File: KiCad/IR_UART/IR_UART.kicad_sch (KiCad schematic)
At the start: 23 parts, among them J1 Conn_01x04, J2 Mounting PTH, J3 Mounting PTH, J4 Mounting PTH, J5 Mounting PTH, Q1 BC817, U1 TSDP34156, U2 74HC132

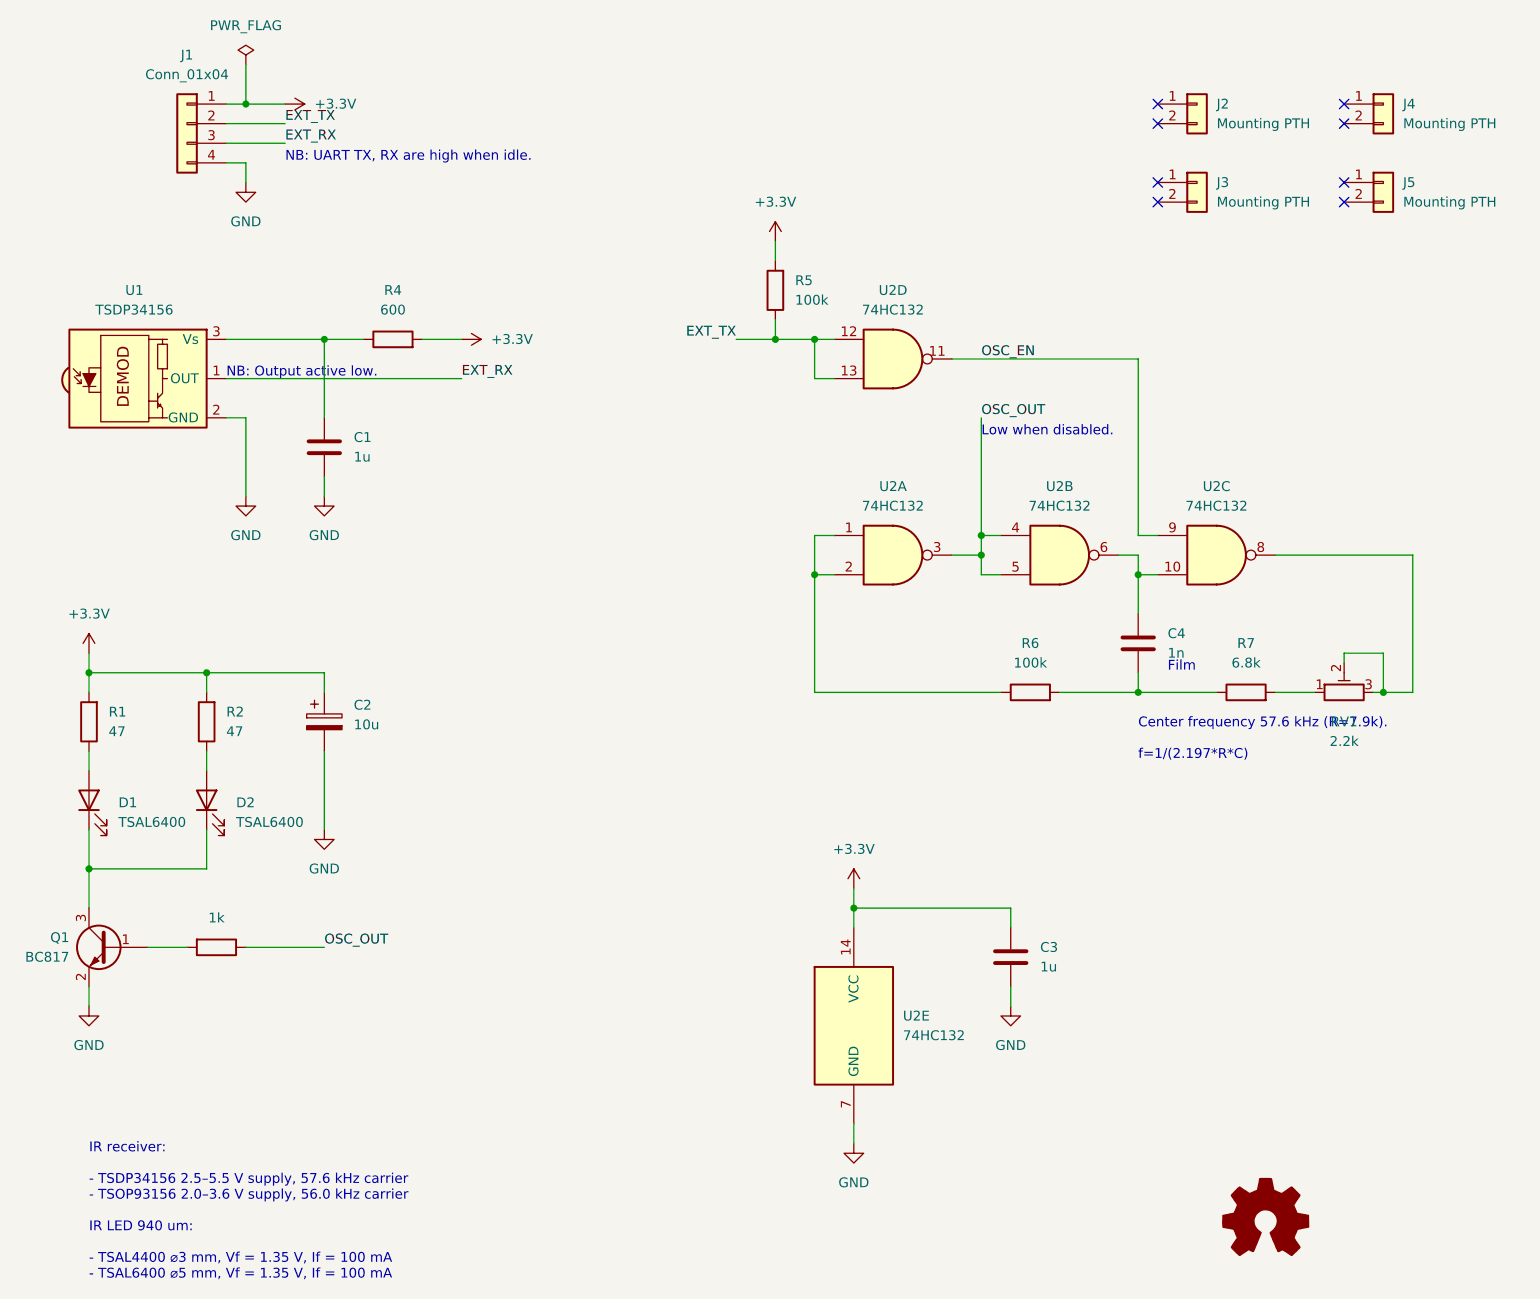
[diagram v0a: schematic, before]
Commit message: Update the schematic and the PCB
- Use 4.7k resistor instead of 6.8k in the timing circuit
- Minor changes to the board, mainly aroung the 4-pin connector
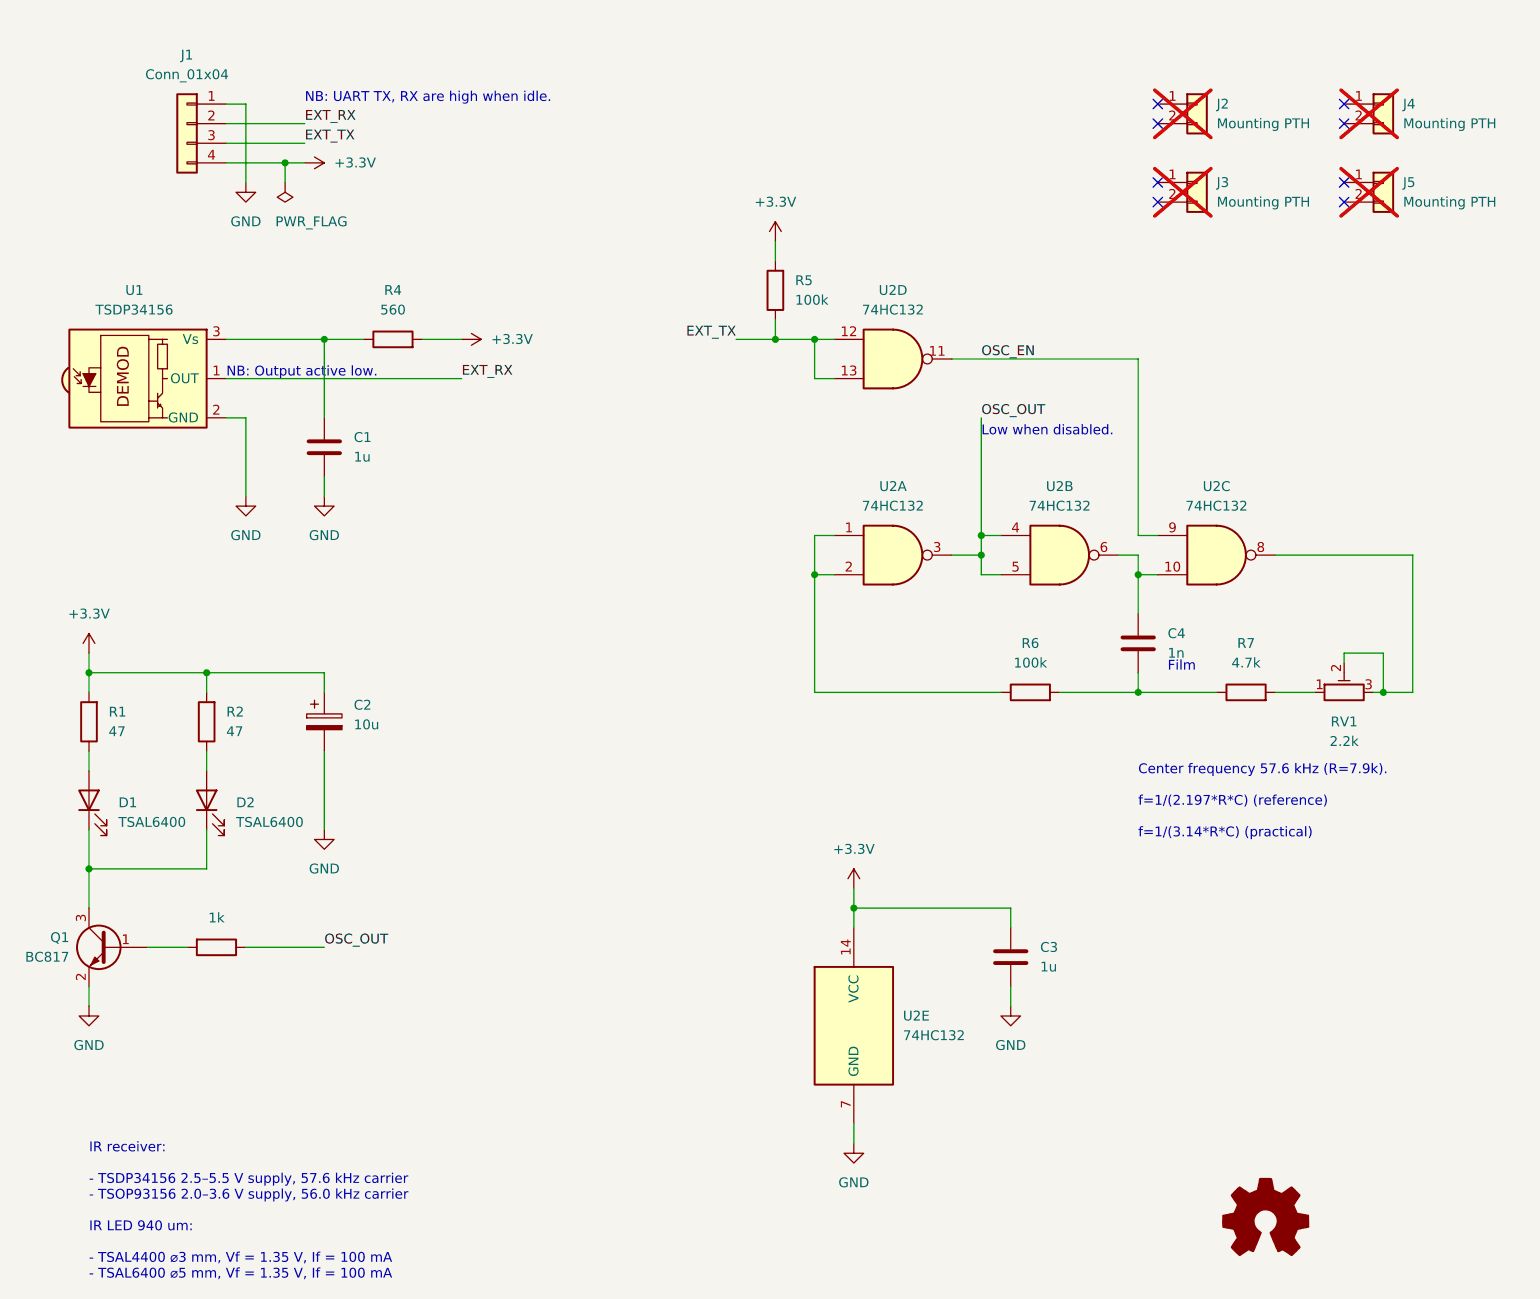
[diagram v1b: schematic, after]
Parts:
- J2, J3, J4, J5: now not fitted; now left out of the parts list
- R4: value 600 -> 560
- R7: value 6.8k -> 4.7k
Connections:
- net +3.3V: now also J1.4 (Pin_4); no longer J1.1 (Pin_1)
- net EXT_RX: now also J1.2 (Pin_2); no longer J1.3 (Pin_3)
- net EXT_TX: now also J1.3 (Pin_3); no longer J1.2 (Pin_2)
- net GND: now also J1.1 (Pin_1); no longer J1.4 (Pin_4)
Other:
- note added: "Center frequency 57.6 kHz (R=7.9k). f=1/(2.197*R*C) (reference) f=1/(3.14*R*C) (practical)"
- note removed: "Center frequency 57.6 kHz (R=7.9k). f=1/(2.197*R*C)"
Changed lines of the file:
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@@
   (title_block
     (title "IR UART 9600 baud")
-    (rev "1")
+    (rev "1.1")
   )
   (junction (at 46.99 102.87) (diameter 0) (color 0 0 0 0)
   )
-  (junction (at 52.07 29.21) (diameter 0) (color 0 0 0 0)
-  )
   (junction (at 62.23 59.69) (diameter 0) (color 0 0 0 0)
   )
@@
   )
   (junction (at 147.32 85.09) (diameter 0) (color 0 0 0 0)
+  )
+  (junction (at 57.15 36.83) (diameter 0) (color 0 0 0 0)
   )
   (junction (at 31.75 102.87) (diameter 0) (color 0 0 0 0)
@@
     (stroke (width 0) (type default))
   )
+  (wire (pts (xy 57.15 36.83) (xy 57.15 39.37))
+    (stroke (width 0) (type default))
+  )
   (wire (pts (xy 167.64 90.17) (xy 170.18 90.17))
     (stroke (width 0) (type default))
@@
     (stroke (width 0) (type default))
   )
-  (wire (pts (xy 49.53 34.29) (xy 57.15 34.29))
+  (wire (pts (xy 49.53 31.75) (xy 59.69 31.75))
     (stroke (width 0) (type default))
   )
@@
     (stroke (width 0) (type default))
   )
+  (wire (pts (xy 57.15 36.83) (xy 59.69 36.83))
+    (stroke (width 0) (type default))
+  )
   (wire (pts (xy 185.42 105.41) (xy 190.5 105.41))
     (stroke (width 0) (type default))
@@
     (stroke (width 0) (type default))
   )
-  (wire (pts (xy 52.07 29.21) (xy 57.15 29.21))
+  (wire (pts (xy 49.53 36.83) (xy 57.15 36.83))
     (stroke (width 0) (type default))
   )
@@
     (stroke (width 0) (type default))
   )
-  (wire (pts (xy 52.07 36.83) (xy 52.07 39.37))
+  (wire (pts (xy 52.07 29.21) (xy 52.07 39.37))
     (stroke (width 0) (type default))
   )
@@
     (stroke (width 0) (type default))
   )
-  (wire (pts (xy 49.53 36.83) (xy 52.07 36.83))
+  (wire (pts (xy 49.53 29.21) (xy 52.07 29.21))
     (stroke (width 0) (type default))
   )
@@
     (stroke (width 0) (type default))
   )
-  (wire (pts (xy 49.53 31.75) (xy 57.15 31.75))
+  (wire (pts (xy 49.53 34.29) (xy 59.69 34.29))
     (stroke (width 0) (type default))
   )
@@
     (stroke (width 0) (type default))
   )
-  (wire (pts (xy 49.53 29.21) (xy 52.07 29.21))
-    (stroke (width 0) (type default))
-  )
   (wire (pts (xy 199.39 105.41) (xy 198.12 105.41))
     (stroke (width 0) (type default))
@@
   )
   (wire (pts (xy 167.64 105.41) (xy 177.8 105.41))
-    (stroke (width 0) (type default))
-  )
-  (wire (pts (xy 52.07 24.13) (xy 52.07 29.21))
     (stroke (width 0) (type default))
   )
@@
     (effects (font (size 1.27 1.27)) (justify left bottom))
   )
-  (text "NB: UART TX, RX are high when idle." (at 57.15 36.83 0)
+  (text "NB: UART TX, RX are high when idle." (at 59.69 29.21 0)
     (effects (font (size 1.27 1.27)) (justify left bottom))
   )
-  (text "Center frequency 57.6 kHz (R=7.9k).\n\nf=1/(2.197*R*C)"
-    (at 167.64 114.3 0)
+  (text "Center frequency 57.6 kHz (R=7.9k).\n\nf=1/(2.197*R*C) (reference)\n\nf=1/(3.14*R*C) (practical)"
+    (at 167.64 124.46 0)
     (effects (font (size 1.27 1.27)) (justify left bottom))
   )
@@
     (effects (font (size 1.27 1.27)) (justify left bottom))
   )
-  (label "EXT_RX" (at 57.15 34.29 0) (fields_autoplaced)
+  (label "EXT_RX" (at 59.69 31.75 0) (fields_autoplaced)
     (effects (font (size 1.27 1.27)) (justify left bottom))
   )
@@
     (effects (font (size 1.27 1.27)) (justify left bottom))
   )
-  (label "EXT_TX" (at 57.15 31.75 0) (fields_autoplaced)
+  (label "EXT_TX" (at 59.69 34.29 0) (fields_autoplaced)
     (effects (font (size 1.27 1.27)) (justify left bottom))
   )
@@
     )
   )
-  (symbol (lib_id "power:PWR_FLAG") (at 52.07 24.13 0) (unit 1)
-    (in_bom yes) (on_board yes) (dnp no) (fields_autoplaced)
-    (property "Reference" "#FLG01" (at 52.07 22.225 0)
-      (effects (font (size 1.27 1.27)) hide)
-    )
-    (property "Value" "PWR_FLAG" (at 52.07 19.05 0)
-      (effects (font (size 1.27 1.27)))
-    )
-    (property "Footprint" "" (at 52.07 24.13 0)
-      (effects (font (size 1.27 1.27)) hide)
-    )
-    (property "Datasheet" "~" (at 52.07 24.13 0)
+  (symbol (lib_id "power:PWR_FLAG") (at 57.15 39.37 180) (unit 1)
+    (in_bom yes) (on_board yes) (dnp no)
+    (property "Reference" "#FLG01" (at 57.15 41.275 0)
+      (effects (font (size 1.27 1.27)) hide)
+    )
+    (property "Value" "PWR_FLAG" (at 55.88 44.45 0)
+      (effects (font (size 1.27 1.27)) (justify right))
+    )
+    (property "Footprint" "" (at 57.15 39.37 0)
+      (effects (font (size 1.27 1.27)) hide)
+    )
+    (property "Datasheet" "~" (at 57.15 39.37 0)
       (effects (font (size 1.27 1.27)) hide)
     )
@@
   )
   (symbol (lib_id "Connector_Generic:Conn_01x02") (at 199.39 29.21 0) (unit 1)
-    (in_bom yes) (on_board yes) (dnp no) (fields_autoplaced)
+    (in_bom no) (on_board yes) (dnp yes) (fields_autoplaced)
     (property "Reference" "J4" (at 201.93 29.21 0)
       (effects (font (size 1.27 1.27)) (justify left))
@@
   )
   (symbol (lib_id "Connector_Generic:Conn_01x02") (at 175.26 39.37 0) (unit 1)
-    (in_bom yes) (on_board yes) (dnp no) (fields_autoplaced)
+    (in_bom no) (on_board yes) (dnp yes) (fields_autoplaced)
     (property "Reference" "J3" (at 177.8 39.37 0)
       (effects (font (size 1.27 1.27)) (justify left))
@@
       (effects (font (size 1.27 1.27)))
     )
-    (property "Value" "6.8k" (at 181.61 101.6 90)
+    (property "Value" "4.7k" (at 181.61 101.6 90)
       (effects (font (size 1.27 1.27)))
     )
@@
   )
   (symbol (lib_id "Connector_Generic:Conn_01x02") (at 199.39 39.37 0) (unit 1)
-    (in_bom yes) (on_board yes) (dnp no) (fields_autoplaced)
+    (in_bom no) (on_board yes) (dnp yes) (fields_autoplaced)
     (property "Reference" "J5" (at 201.93 39.37 0)
       (effects (font (size 1.27 1.27)) (justify left))
@@
   )
   (symbol (lib_id "Connector_Generic:Conn_01x02") (at 175.26 29.21 0) (unit 1)
-    (in_bom yes) (on_board yes) (dnp no) (fields_autoplaced)
+    (in_bom no) (on_board yes) (dnp yes) (fields_autoplaced)
     (property "Reference" "J2" (at 177.8 29.21 0)
       (effects (font (size 1.27 1.27)) (justify left))
@@
       (effects (font (size 1.27 1.27)))
     )
-    (property "Value" "600" (at 71.12 55.88 90)
+    (property "Value" "560" (at 71.12 55.88 90)
       (effects (font (size 1.27 1.27)))
     )
@@
     )
   )
-  (symbol (lib_id "power:+3.3V") (at 57.15 29.21 270) (unit 1)
-    (in_bom yes) (on_board yes) (dnp no) (fields_autoplaced)
-    (property "Reference" "#PWR05" (at 53.34 29.21 0)
-      (effects (font (size 1.27 1.27)) hide)
-    )
-    (property "Value" "+3.3V" (at 60.96 29.21 90)
-      (effects (font (size 1.27 1.27)) (justify left))
-    )
-    (property "Footprint" "" (at 57.15 29.21 0)
-      (effects (font (size 1.27 1.27)) hide)
-    )
-    (property "Datasheet" "" (at 57.15 29.21 0)
-      (effects (font (size 1.27 1.27)) hide)
-    )
+  (symbol (lib_id "power:+3.3V") (at 59.69 36.83 270) (unit 1)
+    (in_bom yes) (on_board yes) (dnp no) (fields_autoplaced)
+    (property "Reference" "#PWR05" (at 55.88 36.83 0)
+      (effects (font (size 1.27 1.27)) hide)
+    )
+    (property "Value" "+3.3V" (at 63.5 36.83 90)
+      (effects (font (size 1.27 1.27)) (justify left))
+    )
+    (property "Footprint" "" (at 59.69 36.83 0)
+      (effects (font (size 1.27 1.27)) hide)
+    )
+    (property "Datasheet" "" (at 59.69 36.83 0)
+      (effects (font (size 1.27 1.27)) hide)
+    )

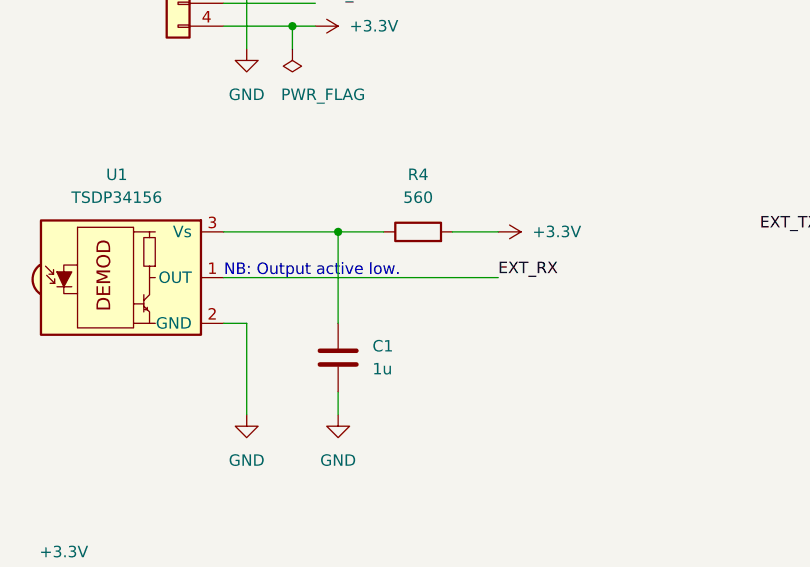
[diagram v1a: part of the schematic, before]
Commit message: Update the schematic to specify IR receiver supply filter to be 100R 4.7uF to fix the slow fronts of the received signal.
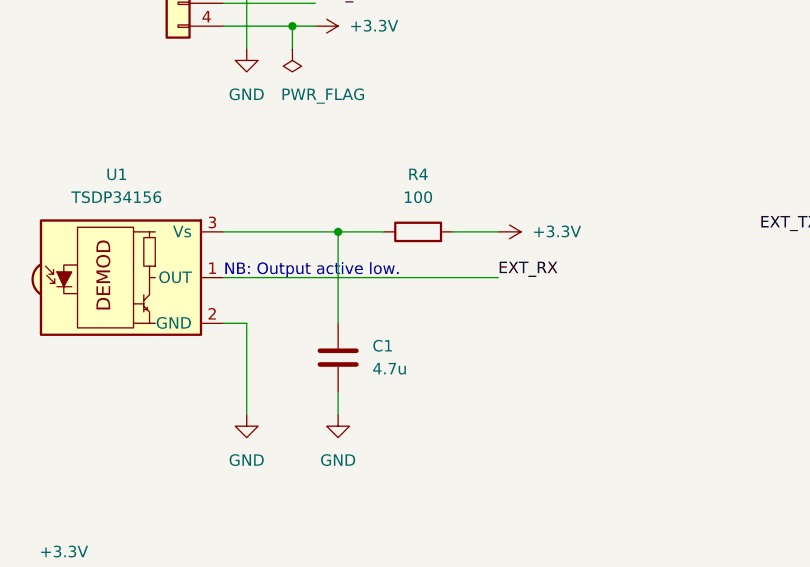
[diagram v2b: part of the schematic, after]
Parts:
- C1: value 1u -> 4.7u
- R4: value 560 -> 100
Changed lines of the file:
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@@
       (effects (font (size 1.27 1.27)) (justify left))
     )
-    (property "Value" "1u" (at 66.04 74.93 0)
+    (property "Value" "4.7u" (at 66.04 74.93 0)
       (effects (font (size 1.27 1.27)) (justify left))
     )
@@
       (effects (font (size 1.27 1.27)))
     )
-    (property "Value" "560" (at 71.12 55.88 90)
-      (effects (font (size 1.27 1.27)))
-    )
+    (property "Value" "100" (at 71.12 55.88 90)
+      (effects (font (size 1.27 1.27)))
+    )
